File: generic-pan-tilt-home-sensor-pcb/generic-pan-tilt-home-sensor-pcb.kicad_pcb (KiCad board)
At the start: 2 copper layers, 15 x 26.9 mm, 10 parts, among them J1 S4B-PH-SM4-TB, U1 AH1806-W

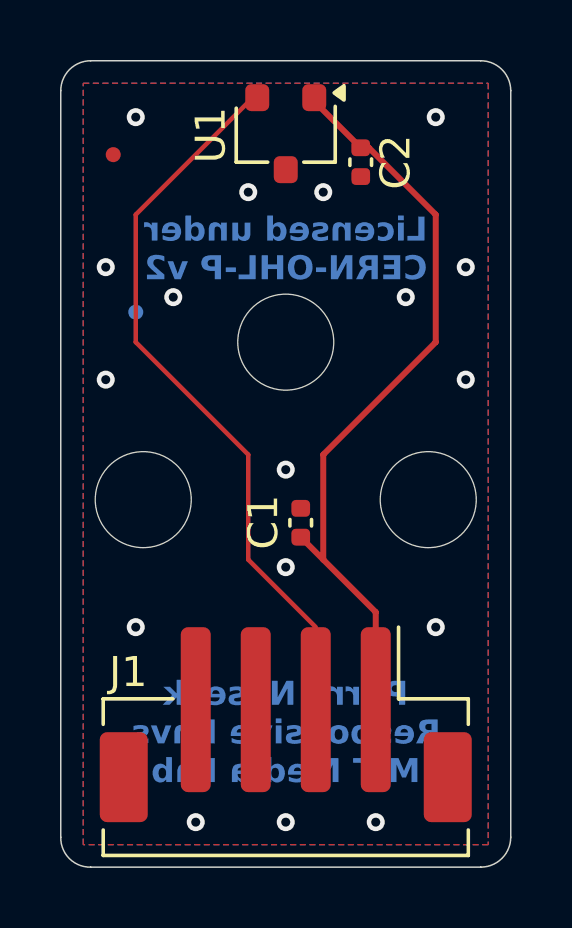
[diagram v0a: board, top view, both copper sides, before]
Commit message: reduce home sensor board 1mm
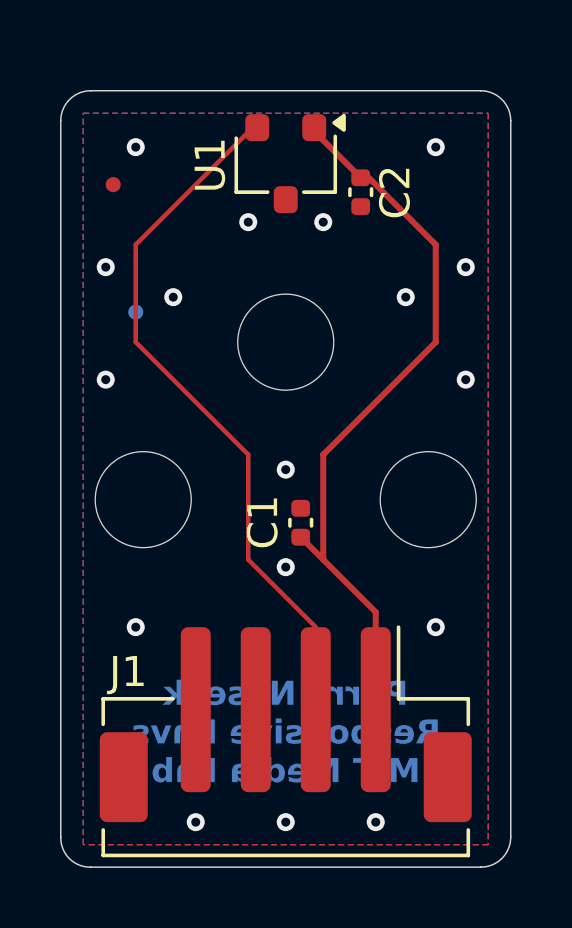
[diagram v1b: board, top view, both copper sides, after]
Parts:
- moved C2 1.00 mm to (107.5, 90.0)
- moved FID1 1.00 mm to (99.2, 89.8)
- moved U1 1.00 mm to (105.0, 89.0)
- moved SYM1 0.25 mm to (105.0, 103.0)
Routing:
- net +3V3: track 25.6 -> 24.2 mm
- net /REF_1: track 21.9 -> 20.8 mm
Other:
- board size 15 x 26.9 mm -> 15 x 25.9 mm
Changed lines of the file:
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@@
 	(footprint "Package_TO_SOT_SMD:SC-59"
 		(layer "F.Cu")
-		(at 105 88.05 -90)
+		(at 105 89.05 -90)
 		(descr "SC-59, https://lib.chipdip.ru/images/import_diod/original/SOT-23_SC-59.jpg")
 		(tags "SC-59")
@@
 		)
 		(fp_text user "${REFERENCE}"
-			(at 0 0 360)
+			(at 0 0 0)
 			(layer "F.Fab")
 			(effects
@@
 	(footprint "Fiducial:Fiducial_0.5mm_Mask1mm"
 		(layer "F.Cu")
-		(at 99.25 88.75)
+		(at 99.25 89.75)
 		(descr "Circular Fiducial, 0.5mm bare copper, 1mm soldermask opening (Level C)")
 		(tags "fiducial")
@@
 	(footprint "Capacitor_SMD:C_0402_1005Metric"
 		(layer "F.Cu")
-		(at 107.5 89 -90)
+		(at 107.5 90 -90)
 		(descr "Capacitor SMD 0402 (1005 Metric), square (rectangular) end terminal, IPC_7351 nominal, (Body size source: IPC-SM-782 page 76, https://www.pcb-3d.com/wordpress/wp-content/uploads/ipc-sm-782a_amendment_1_and_2.pdf), generated with kicad-footprint-generator")
 		(tags "capacitor")
@@
 		(tags "connector JST PH vertical")
 		(property "Reference" "J1"
-			(at 5.25 1.75 360)
+			(at 5.25 1.75 0)
 			(layer "F.SilkS")
 			(effects
@@
 		)
 		(property "Value" "S4B-PH-SM4-TB"
-			(at 0 4.45 360)
+			(at 0 4.45 0)
 			(layer "F.Fab")
 			(effects
@@
 		)
 		(fp_text user "${REFERENCE}"
-			(at 0 -1 360)
+			(at 0 -1 0)
 			(layer "F.Fab")
 			(effects
@@
 	(footprint "Symbol:OSHW-Logo2_7.3x6mm_SilkScreen"
 		(layer "B.Cu")
-		(at 105 103.25 180)
+		(at 105 103 180)
 		(descr "Open Source Hardware Symbol")
 		(tags "Logo Symbol OSHW")
@@
 	(gr_line
 		(start 112.5 111.5)
-		(end 112.5 86.62)
+		(end 112.5 87.62)
 		(stroke
 			(width 0.05)
@@
 	)
 	(gr_arc
-		(start 97.5 86.62)
-		(mid 97.792893 85.912893)
-		(end 98.5 85.62)
+		(start 97.5 87.62)
+		(mid 97.792893 86.912893)
+		(end 98.5 86.62)
 		(stroke
 			(width 0.05)
@@
 	)
 	(gr_arc
-		(start 111.5 85.62)
-		(mid 112.207107 85.912893)
-		(end 112.5 86.62)
+		(start 111.5 86.62)
+		(mid 112.207107 86.912893)
+		(end 112.5 87.62)
 		(stroke
 			(width 0.05)
@@
 	)
 	(gr_line
-		(start 97.5 86.62)
+		(start 97.5 87.62)
 		(end 97.5 111.5)
 		(stroke
@@
 	)
 	(gr_line
-		(start 111.5 85.62)
-		(end 98.5 85.62)
+		(start 111.5 86.62)
+		(end 98.5 86.62)
 		(stroke
 			(width 0.05)
@@
 		)
 		(layer "Edge.Cuts")
-	)
-	(gr_text "Licensed under\nCERN-OHL-P v2"
-		(at 105 93 0)
-		(layer "B.Cu")
-		(effects
-			(font
-				(size 0.8 0.8)
-				(thickness 0.2)
-				(bold yes)
-			)
-			(justify bottom mirror)
-		)
 	)
 	(gr_text "Perry Naseck\nResponsive Envs\nMIT Media Lab"
@@
 	)
 	(gr_text "Rev: ${KIBOT_GIT_DESCRIBE}\n${KIBOT_GIT_DATE}\n${KITBOT_RUN_DATE}"
-		(at 105 90.25 0)
+		(at 105 90.5 0)
 		(layer "B.SilkS")
 		(effects
@@
 		(layer "User.1")
 		(pts
-			(xy 105 95) (xy 112.5 85.62)
+			(xy 105 95) (xy 112.5 86.62)
 		)
 		(height 10)
 		(orientation 1)
-		(gr_text "9.3800 mm"
-			(at 113.85 90.31 90)
+		(gr_text "8.3800 mm"
+			(at 113.85 90.81 90)
 			(layer "User.1")
 			(effects
@@
 	)
 	(via
-		(at 100 87.5)
+		(at 100 88.5)
 		(size 0.6)
 		(drill 0.3)
@@
 	)
 	(via
-		(at 106.25 90)
+		(at 106.25 91)
 		(size 0.6)
 		(drill 0.3)
@@
 	)
 	(via
-		(at 110 87.5)
+		(at 110 88.5)
 		(size 0.6)
 		(drill 0.3)
@@
 	)
 	(via
-		(at 103.75 90)
+		(at 103.75 91)
 		(size 0.6)
 		(drill 0.3)
@@
 	)
 	(segment
-		(start 110 90.75)
-		(end 107.77 88.52)
+		(start 110 91.75)
+		(end 107.77 89.52)
 		(width 0.2)
 		(layer "F.Cu")
@@
 	)
 	(segment
-		(start 107.77 88.52)
-		(end 107.5 88.52)
-		(width 0.2)
-		(layer "F.Cu")
-		(net 2)
-	)
-	(segment
-		(start 110 95)
-		(end 110 90.75)
-		(width 0.2)
-		(layer "F.Cu")
-		(net 2)
-	)
-	(segment
-		(start 105.95 86.97)
-		(end 107.5 88.52)
+		(start 105.95 87.97)
+		(end 107.5 89.52)
 		(width 0.2)
 		(layer "F.Cu")
@@
 	)
 	(segment
+		(start 110 91.75)
+		(end 110 95)
+		(width 0.2)
+		(layer "F.Cu")
+		(net 2)
+	)
+	(segment
 		(start 106.25 98.75)
 		(end 110 95)
@@
 	)
 	(segment
-		(start 105.95 86.85)
-		(end 105.95 86.97)
-		(width 0.2)
-		(layer "F.Cu")
-		(net 2)
-	)
-	(segment
-		(start 100 95)
-		(end 100 90.75)
-		(width 0.15)
-		(layer "F.Cu")
-		(net 3)
-	)
-	(segment
-		(start 100 90.75)
-		(end 103.9 86.85)
+		(start 100 91.75)
+		(end 103.9 87.85)
 		(width 0.15)
 		(layer "F.Cu")
@@
 	)
 	(segment
-		(start 103.9 86.85)
-		(end 104.05 86.85)
+		(start 100 91.75)
+		(end 100 95)
 		(width 0.15)
 		(layer "F.Cu")
@@
 		(polygon
 			(pts
-				(xy 111.75 86.37) (xy 111.75 111.75) (xy 98.25 111.75) (xy 98.25 86.37)
-			)
-		)
+				(xy 111.75 87.37) (xy 111.75 111.75) (xy 98.25 111.75) (xy 98.25 87.37)
+			)
+		)

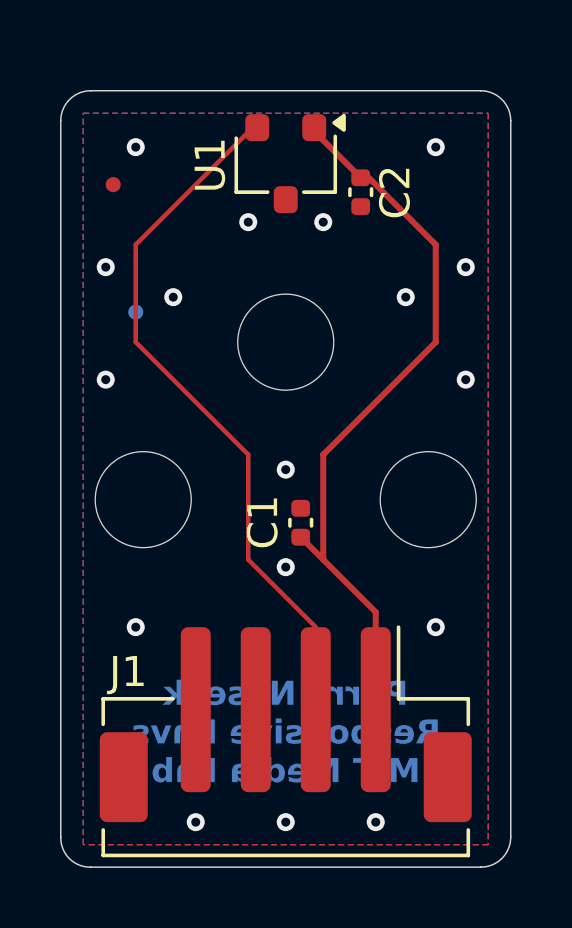
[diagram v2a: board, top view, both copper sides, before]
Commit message: home sensor 0603 cap, flip conn, more part numbers
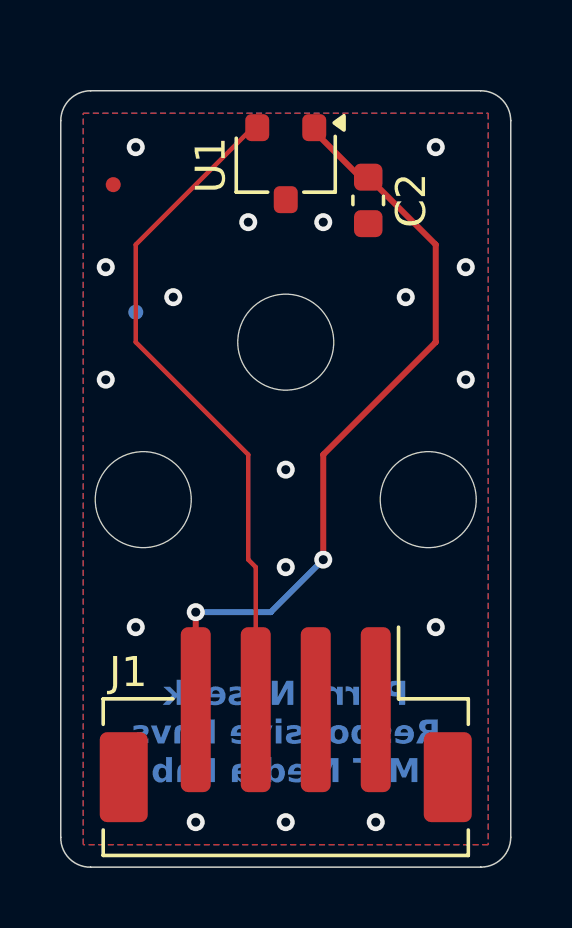
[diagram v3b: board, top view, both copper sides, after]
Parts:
- removed C1: 1µF 16V, Capacitor_SMD:C_0402_1005Metric
- C2: value 0.1µF 16V -> 0.1µF; footprint Capacitor_SMD:C_0402_1005Metric -> Capacitor_SMD:C_0603_1608Metric
- J1: value S4B-PH-SM4-TB -> B4B-PH-SM4-TB
- U1: value AH1806-W -> AH1806-W-7
- moved C2 0.37 mm to (107.8, 90.3)
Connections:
- J1 pad 1: +3V3 -> GND
- J1 pad 2: /REF_1 -> /REF_2
- J1 pad 3: /REF_2 -> /REF_1
- J1 pad 4: GND -> +3V3
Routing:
- net /REF_1: track 20.8 -> 22.7 mm
- net +3V3: track 24.2 -> 25.6 mm, vias 0 -> 2

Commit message: home sensor rev silk length
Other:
- board text added: "${KIBOT_GIT_DESCRIBE} ${KIBOT_GIT_DATE} ${KITBOT_RUN_DATE}"
- board text removed: "Rev: ${KIBOT_GIT_DESCRIBE} ${KIBOT_GIT_DATE} ${KITBOT_RUN_DATE}"
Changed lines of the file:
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@@
 		)
 	)
-	(gr_text "Rev: ${KIBOT_GIT_DESCRIBE}\n${KIBOT_GIT_DATE}\n${KITBOT_RUN_DATE}"
+	(gr_text "${KIBOT_GIT_DESCRIBE}\n${KIBOT_GIT_DATE}\n${KITBOT_RUN_DATE}"
 		(at 105 90.5 0)
 		(layer "B.SilkS")
